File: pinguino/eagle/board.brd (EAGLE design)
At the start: 100 x 50.8 mm, 21 parts, among them U1 PIC18F2550-I/SP, U2 LM7805, X1 22MHZ

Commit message: pinguino board
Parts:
- removed U2: LM7805, v-reg-3:TO220S
- added IC1: (no value), v-reg:78XXL
- moved R1 61.3 mm to (87.6, 82.5), turned to 90 degrees
- moved R2 56.4 mm to (10.2, 87.6)
- moved RUN 50.8 mm to (63.5, 71.1)
- moved JP1 35.1 mm to (61.0, 86.4), turned to 90 degrees
- moved C1 33.2 mm to (43.2, 57.1), turned to 270 degrees
- moved C2 33.1 mm to (19.1, 63.5), turned to 270 degrees
- moved R3 29.0 mm to (15.2, 73.7), turned to 90 degrees
- moved C4 28.5 mm to (67.3, 63.5), turned to 90 degrees
- moved X1 25.7 mm to (41.9, 64.8), turned to 0 degrees
- moved JP3 24.7 mm to (24.1, 52.1)
- moved C3 24.7 mm to (59.7, 54.6)
- moved JP5 24.7 mm to (47.0, 52.1)
- moved JP4 23.6 mm to (39.4, 96.5)
- moved JP6 23.6 mm to (54.6, 96.5)
- moved U1 22.6 mm to (38.1, 73.7)
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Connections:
- removed net N$9: JP3.4
- net GND: now also IC1.GND; no longer U2.1
- net N$10: now also IC1.IN; no longer U2.3
- net N$7: now also IC1.OUT; no longer U2.2
- net PIN5: now also JP3.4
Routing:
- net GND: track 0.00 -> 202.5 mm
- net VCC: track 0.00 -> 117.7 mm
- net N$7: track 0.00 -> 116.3 mm
- net N$8: track 0.00 -> 49.8 mm, vias 0 -> 2
- net D-: track 0.00 -> 48.4 mm
- net D+: track 0.00 -> 48.2 mm
- net PIN6: track 0.00 -> 45.5 mm, vias 0 -> 2
- net N$1: track 0.00 -> 40.8 mm
- net N$4: track 0.00 -> 35.9 mm
- net N$3: track 0.00 -> 25.8 mm
- net N$10: track 0.00 -> 23.8 mm
- net PIN27: track 0.00 -> 19.2 mm
- net PIN23: track 0.00 -> 19.2 mm
- net PIN22: track 0.00 -> 19.2 mm
- net PIN18: track 0.00 -> 19.2 mm
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- added copper zone on layer 16, net GND
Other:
- board size 100 x 50.8 mm -> 104.1 x 51.7 mm

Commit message: correcao de layout
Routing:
- net GND: track 202.5 -> 271.3 mm
- net N$7: track 116.3 -> 131.4 mm
- net N$8: track 49.8 -> 58.0 mm
- net N$10: track 23.8 -> 20.1 mm
- net D+: track 48.2 -> 47.0 mm
- net N$4: track 35.9 -> 36.9 mm
- net N$1: track 40.8 -> 41.0 mm, vias 0 -> 2
- net PIN6: vias 2 -> 6
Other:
- board text added: "Pinguino"

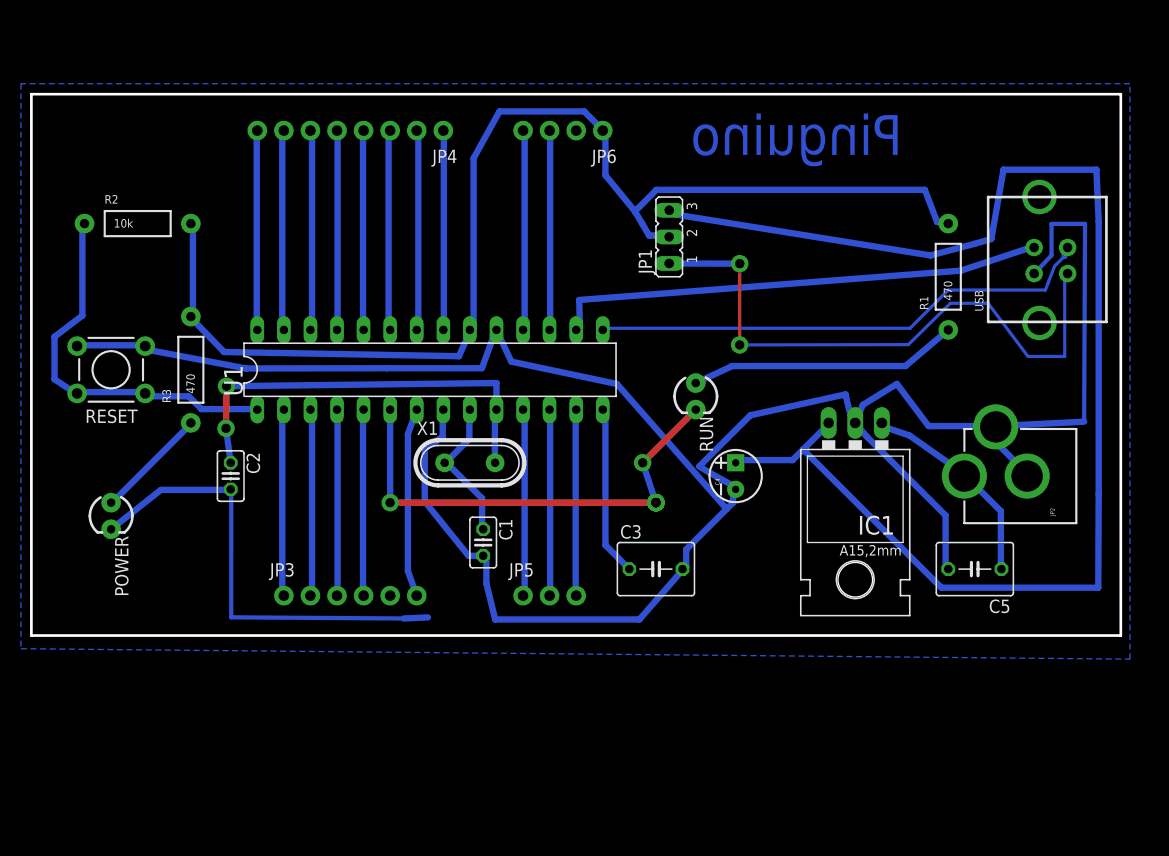
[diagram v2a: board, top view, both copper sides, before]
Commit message: melhorias de layout
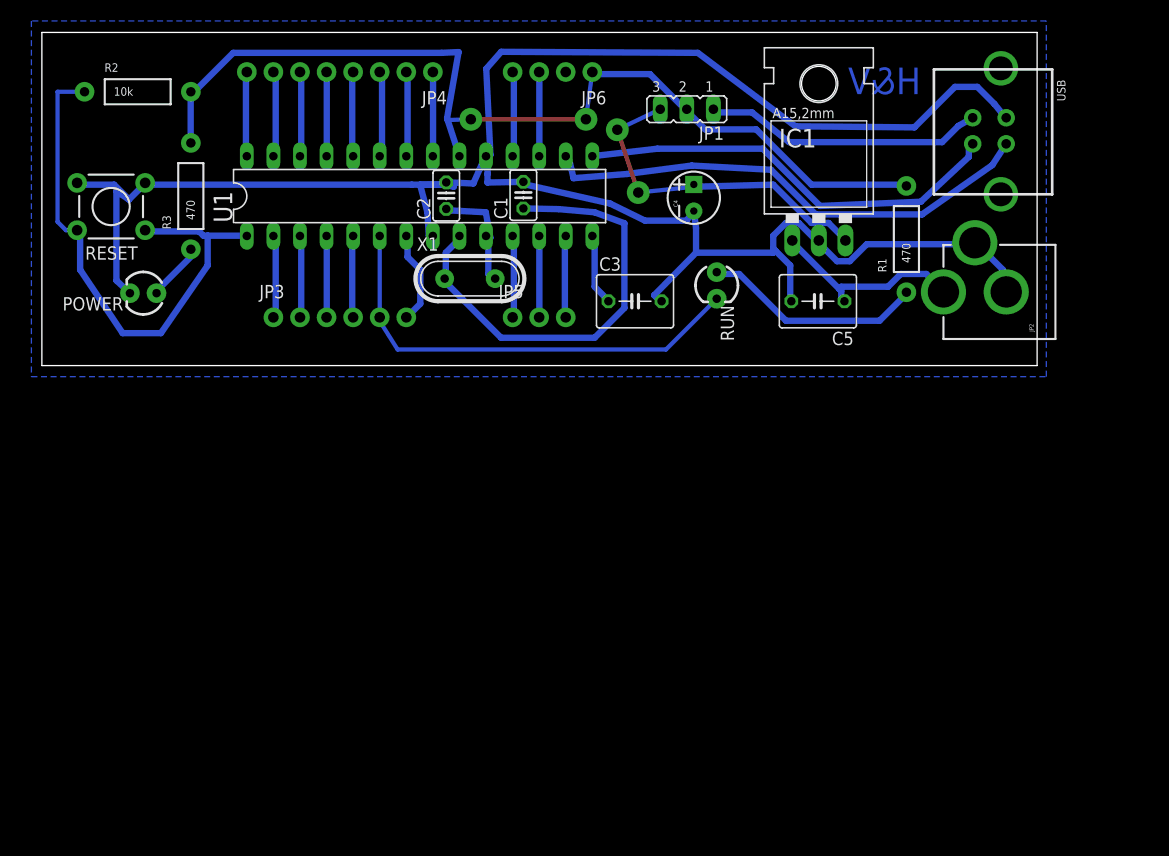
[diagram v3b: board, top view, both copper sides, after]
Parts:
- moved C2 33.8 mm to (39.6, 90.3), turned to 90 degrees
- moved C1 33.4 mm to (47.0, 90.3), turned to 90 degrees
- moved C5 29.7 mm to (75.2, 80.2)
- moved C4 26.9 mm to (63.3, 90.1)
- moved JP3 26.6 mm to (23.1, 78.7)
- moved JP5 26.6 mm to (46.0, 78.7)
- moved C3 25.7 mm to (57.7, 80.2)
- moved IC1 25.3 mm to (75.3, 89.8), turned to 0 degrees
- moved POWER 21.5 mm to (10.7, 81.0), turned to 180 degrees
- moved JP2 17.7 mm to (100.9, 81.1)
- moved X1 17.6 mm to (41.9, 82.4)
- moved U1 16.6 mm to (37.1, 90.3)
- moved R3 16.6 mm to (15.2, 90.3)
- moved RESET 15.6 mm to (7.62, 89.3)
- moved R2 12.6 mm to (10.2, 100.2)
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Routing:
- net N$7: track 131.4 -> 33.2 mm, vias 0 -> 2
- net GND: track 271.3 -> 204.2 mm
- net N$8: track 58.0 -> 26.9 mm, vias 2 -> 0
- net N$1: track 41.0 -> 11.4 mm, vias 2 -> 0
- net N$2: track 14.0 -> 43.4 mm
- net VCC: track 117.9 -> 94.6 mm, vias 0 -> 2
- net N$4: track 36.9 -> 52.8 mm
- net PIN18: track 19.2 -> 8.13 mm
- net PIN22: track 19.2 -> 8.13 mm
- net PIN26: track 19.2 -> 8.13 mm
- net PIN25: track 19.1 -> 8.05 mm
- net PIN21: track 19.1 -> 8.05 mm
- net PIN17: track 19.1 -> 8.05 mm
- net PIN28: track 19.1 -> 8.09 mm
- net PIN24: track 19.1 -> 8.09 mm
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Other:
- board size 104.1 x 51.7 mm -> 95.1 x 31.8 mm
- board text added: "H&V"
- board text removed: "Pinguino"

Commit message: menor proporcao
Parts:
- X1: value 22MHZ -> 20MHZ
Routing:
- net GND: track 204.2 -> 210.3 mm
- net D+: track 48.1 -> 46.3 mm
- net N$2: track 43.4 -> 45.1 mm
- net D-: track 41.6 -> 40.2 mm
- net N$3: track 21.3 -> 22.4 mm
- net VCC: track 94.6 -> 93.6 mm
- net N$8: track 26.9 -> 27.8 mm
- net N$7: track 33.2 -> 32.4 mm

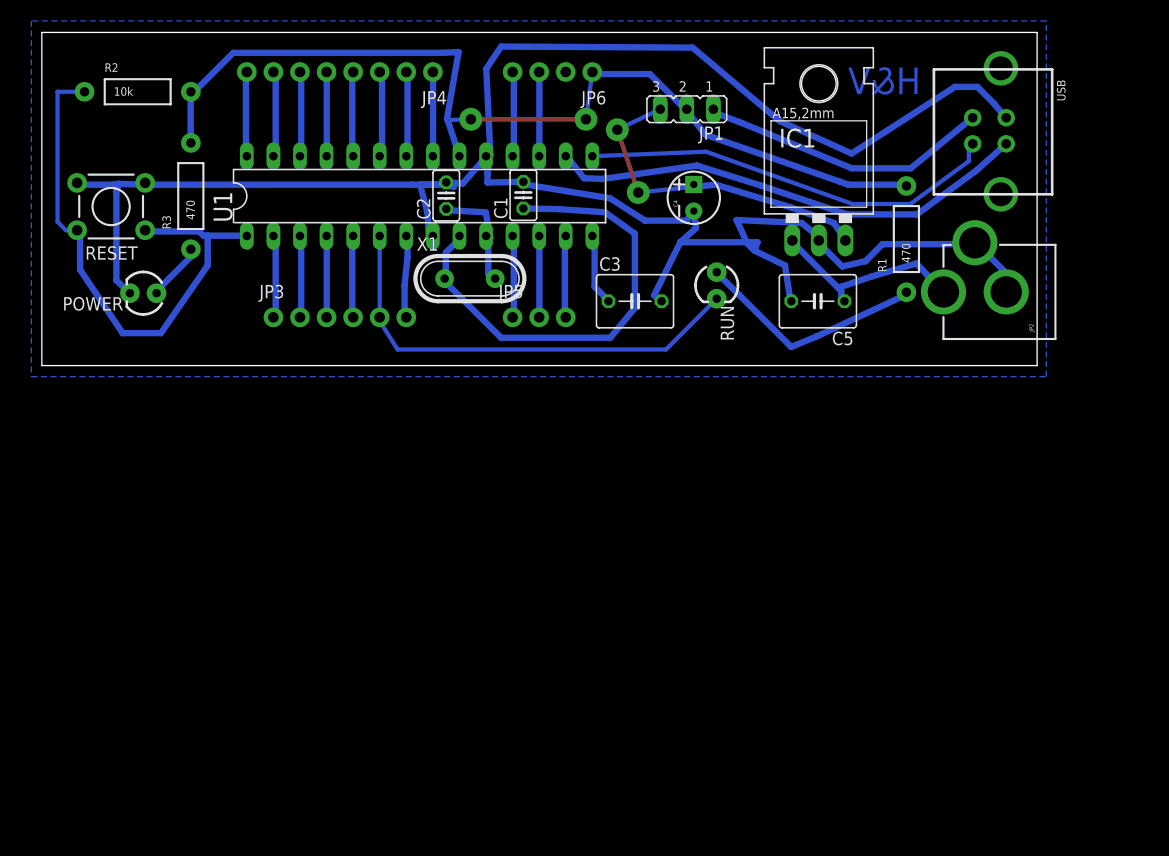
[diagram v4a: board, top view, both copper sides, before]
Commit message: remocao de projeto nao usado atualizando projeto final eagle
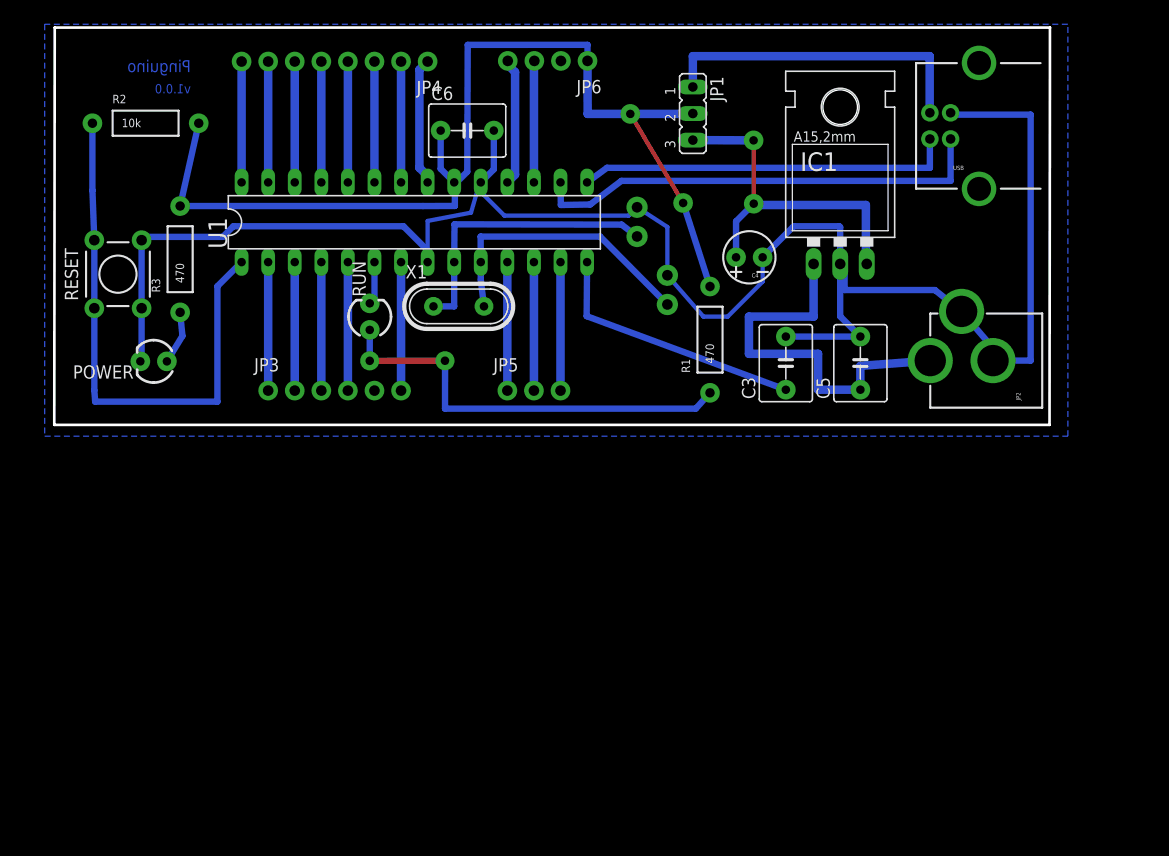
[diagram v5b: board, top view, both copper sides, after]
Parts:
- added C6: 100nf, rcl:C050-050X075
- C1, C2: device rcl:C025-025X050 -> SparkFun-Capacitors:CAP-PTH-SMALL-KIT
- USB: value POWER -> USB-B; device SparkFun-Connectors:USB-B-PTH-VERTICAL -> SparkFun-Connectors:USB-B-PTH
- moved RUN 33.3 mm to (32.3, 78.7), turned to 90 degrees
- moved C2 23.0 mm to (60.8, 81.3), flipped to the bottom
- moved R1 21.1 mm to (64.9, 76.5)
- moved C3 15.6 mm to (72.1, 74.3), turned to 90 degrees
- moved USB 11.7 mm to (87.9, 97.0), turned to 180 degrees
- moved C1 11.2 mm to (57.9, 87.8), flipped to the bottom
- moved C4 7.78 mm to (68.6, 84.4), turned to 180 degrees
- moved C5 7.18 mm to (79.2, 74.3), turned to 90 degrees
- moved JP3 7.02 mm to (22.6, 71.7)
- moved JP5 7.02 mm to (45.5, 71.7)
- moved JP2 6.68 mm to (99.6, 74.5)
- moved POWER 6.59 mm to (11.7, 74.5)
- moved RESET 6.50 mm to (8.27, 82.8), turned to 90 degrees
- moved R3 6.12 mm to (14.2, 84.2)
- moved R2 3.10 mm to (10.9, 97.2)
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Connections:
- net GND: now also C6.2
- net VCC: now also C6.1
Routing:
- net PIN6: track 43.9 -> 4.20 mm
- net GND: track 210.3 -> 179.2 mm
- net N$3: track 22.4 -> 41.1 mm, vias 0 -> 2
- net PIN14: track 6.83 -> 25.5 mm
- net N$10: track 19.5 -> 37.8 mm
- net N$2: track 45.1 -> 27.7 mm
- net N$1: track 11.4 -> 27.2 mm
- net VCC: track 93.6 -> 102.9 mm
- net PIN4: track 7.78 -> 12.3 mm
- net PIN12: track 7.78 -> 12.3 mm
- net PIN5: track 7.82 -> 12.3 mm
- net PIN13: track 7.82 -> 12.3 mm
- net PIN11: track 7.86 -> 12.3 mm
- net PIN3: track 7.86 -> 12.3 mm
- net PIN2: track 7.99 -> 12.3 mm
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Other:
- board size 95.1 x 31.8 mm -> 95.2 x 38 mm
- board text added: "Pinguino"
- board text added: "v1.0.0"
- board text removed: "H&V"
